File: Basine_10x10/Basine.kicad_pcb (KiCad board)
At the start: 2 copper layers, 100 x 100 mm, 98 parts, among them J1 2060-451/998-404, J10 2060-451/998-404, J11 2060-451/998-404, J12 2060-451/998-404, J13 2060-451/998-404, J14 2060-451/998-404, J15 2060-451/998-404, J16 2060-451/998-404, J2 2060-451/998-404, J3 2060-451/998-404, J4 2060-451/998-404, J5 2060-451/998-404, J6 2060-451/998-404, J7 2060-451/998-404, J8 2060-451/998-404, J9 2060-451/998-404, U1 SRV05-4, U17 TPS5430DDA, U4 SN65HVD230

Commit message: 10x10
tentative de fabrication
pénurie spring clamp à gérer
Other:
- board text added: "0V"
- board text added: "24V"
- board text added: "3V3"
- board text added: "5V"
- board text added: "CAN"
- board text added: "H"
- board text added: "L"

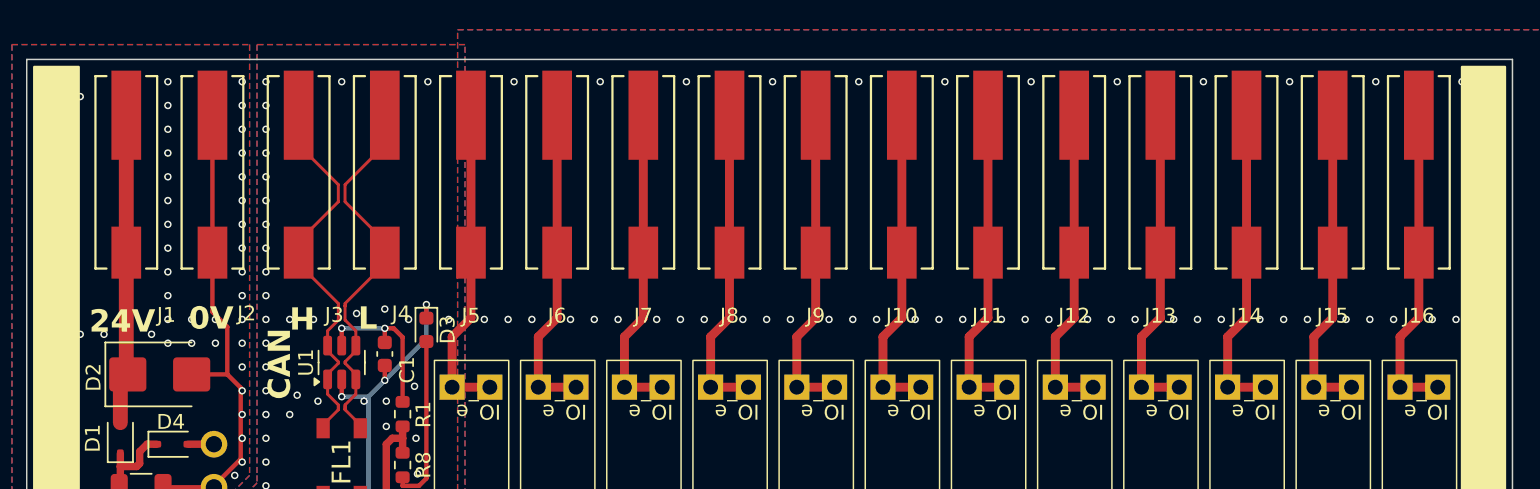
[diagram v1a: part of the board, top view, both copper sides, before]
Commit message: 10x10
chgt connecteur wago
fabrication
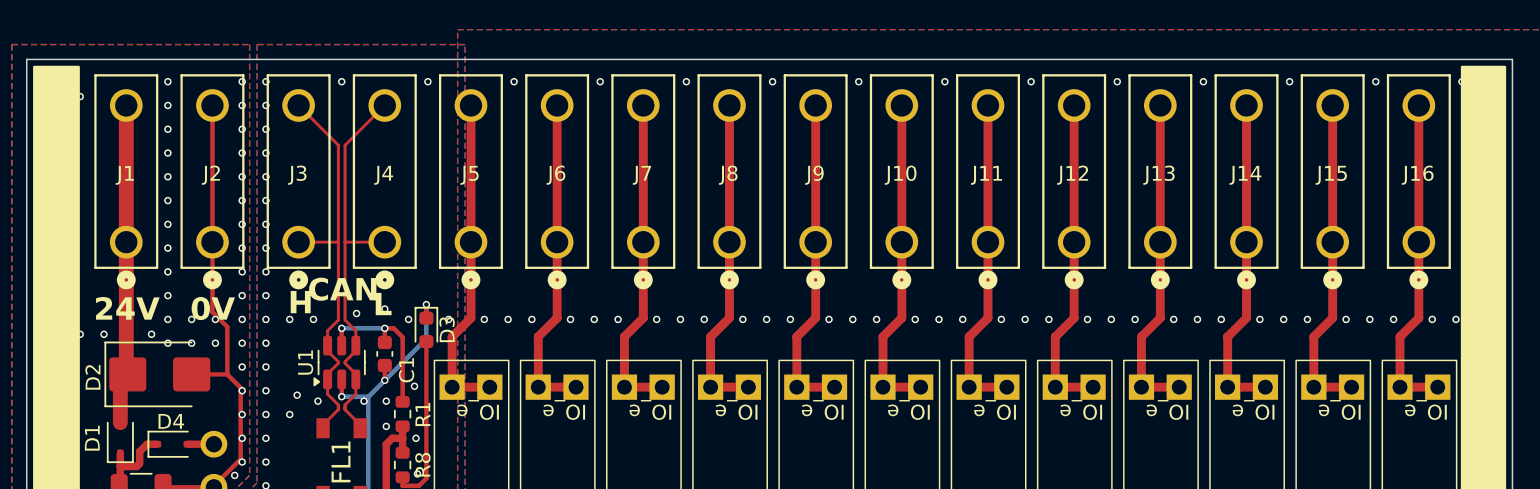
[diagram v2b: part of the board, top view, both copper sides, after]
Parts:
- J1, J10, J11, J12, J13, J14, J15, J16, J2, J3, J4, J5, J6, J7, J8, J9: footprint Chimere_comps:CONN_2060-451_998-404_WAGO -> Chimere_comps:CONN_2060-1451_998-404_WAGO
- moved J10 4.70 mm to (158.9, 112.3), turned to 0 degrees
- moved J5 4.70 mm to (129.9, 112.3), turned to 0 degrees
- moved J6 4.70 mm to (135.7, 112.3), turned to 0 degrees
- moved J7 4.70 mm to (141.5, 112.3), turned to 0 degrees
- moved J8 4.70 mm to (147.3, 112.3), turned to 0 degrees
- moved J9 4.70 mm to (153.1, 112.3), turned to 0 degrees
- moved J1 4.70 mm to (106.7, 112.3), turned to 0 degrees
- moved J11 4.70 mm to (164.7, 112.3), turned to 0 degrees
- moved J12 4.70 mm to (170.5, 112.3), turned to 0 degrees
- moved J13 4.70 mm to (176.3, 112.3), turned to 0 degrees
- moved J14 4.70 mm to (182.1, 112.3), turned to 0 degrees
- moved J15 4.70 mm to (187.9, 112.3), turned to 0 degrees
- moved J16 4.70 mm to (193.7, 112.3), turned to 0 degrees
- moved J2 4.70 mm to (112.5, 112.3), turned to 0 degrees
- moved J3 4.70 mm to (118.3, 112.3), turned to 0 degrees
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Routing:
- net CAN_N: track 26.3 -> 27.4 mm
- net CAN_P: track 26.3 -> 27.4 mm
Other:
- board text removed: "CAN_H"
- board text removed: "CAN_L"

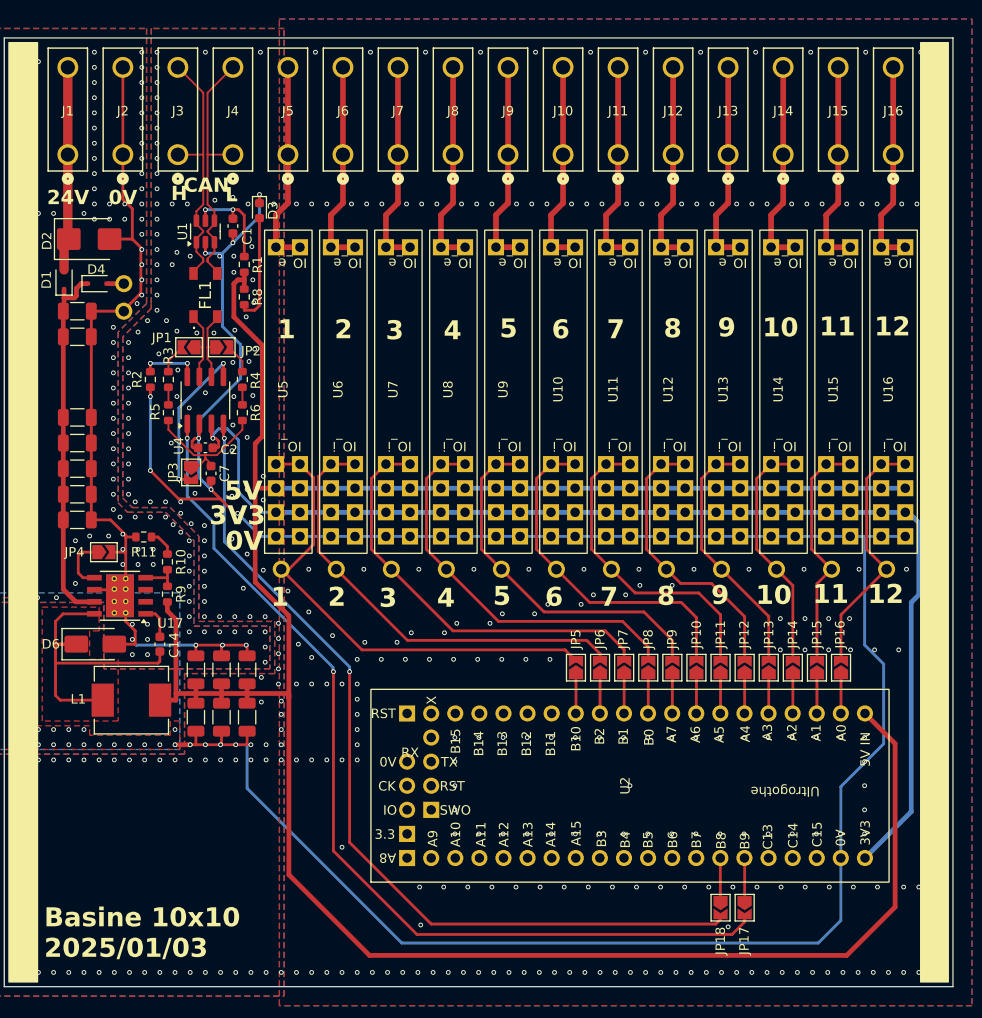
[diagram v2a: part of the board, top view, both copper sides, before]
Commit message: passage au pas de 2,54mm pour toutes les allumettes
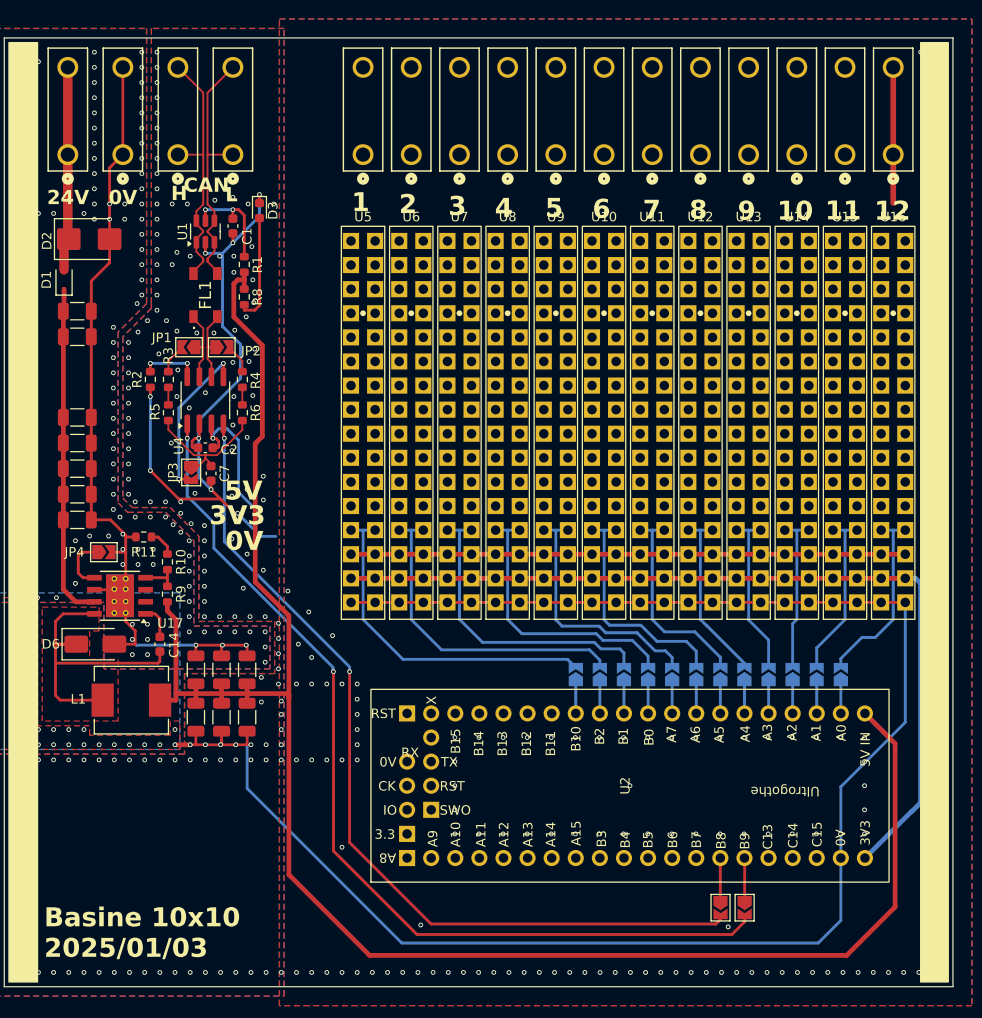
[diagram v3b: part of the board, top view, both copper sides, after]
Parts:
- removed D4: 1N5819WS, Diode_SMD:D_SOD-323
- removed TP1, TP10, TP11, TP12, TP13, TP14, TP2, TP3, TP4, TP5, TP6, TP7, TP8, TP9: TestPoint, Chimere_comps:Pastille
- JP10, JP11, JP12, JP13, JP14, JP15, JP16, JP5, JP6, JP7, JP8, JP9: moved to B.Cu
- moved U5 10.5 mm to (137.8, 144.3)
- moved U6 10.0 mm to (142.9, 144.3)
- moved U7 9.51 mm to (148.0, 144.3)
- moved U8 9.03 mm to (153.1, 144.3)
- moved U9 8.59 mm to (158.1, 144.3)
- moved U10 8.19 mm to (163.2, 144.3)
- moved J5 7.92 mm to (137.8, 112.3)
- moved U11 7.84 mm to (168.3, 144.3)
- moved U12 7.53 mm to (173.4, 144.3)
- moved U13 7.29 mm to (178.5, 144.3)
- moved J6 7.20 mm to (142.9, 112.3)
- moved U14 7.11 mm to (183.5, 144.3)
- moved U15 7.00 mm to (188.6, 144.3)
- moved U16 6.96 mm to (193.7, 144.3)
- moved J7 6.48 mm to (148.0, 112.3)
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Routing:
- net Net-(J7-Pin_1): track 21.4 -> 0.00 mm
- net Net-(J12-Pin_1): track 21.4 -> 0.00 mm
- net Net-(J8-Pin_1): track 21.4 -> 0.00 mm
- net Net-(J5-Pin_1): track 21.4 -> 0.00 mm
- net Net-(J15-Pin_1): track 21.4 -> 0.00 mm
- net Net-(J13-Pin_1): track 21.4 -> 0.00 mm
- net Net-(J10-Pin_1): track 21.4 -> 0.00 mm
- net Net-(J9-Pin_1): track 21.4 -> 0.00 mm
- net Net-(J6-Pin_1): track 21.4 -> 0.00 mm
- net Net-(J14-Pin_1): track 21.4 -> 0.00 mm
- net Net-(J11-Pin_1): track 21.4 -> 0.00 mm
- net 0V: track 356.8 -> 336.8 mm, vias 606 -> 490
- net 3V3: track 123.7 -> 107.6 mm
- net Net-(JP5-B): track 51.1 -> 36.5 mm
- net Net-(JP6-B): track 47.2 -> 34.4 mm
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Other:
- board text removed: "+"
- board text removed: "-"
- board text removed: "autre source"

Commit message: Basine 10x10 : enlever DCDC et CAN
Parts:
- removed C1, C2: 100nF 50V X7R, Capacitor_SMD:C_0603_1608Metric
- removed C10, C11, C15, C18, C19, C3, C4, C8, C9: 10uF 50V, Capacitor_SMD:C_1206_3216Metric
- removed C12, C13, C16, C17: 47uF 10V X5R, Capacitor_SMD:C_1206_3216Metric
- removed C14, C7: 10nF 50V X7R, Capacitor_SMD:C_0603_1608Metric
- removed D1: 1N5819WS, Diode_SMD:D_SOD-323
- removed D2: SMBJ30CA, Diode_SMD:D_SMB
- removed D3: LED, LED_SMD:LED_0603_1608Metric
- removed D6: SS54, Diode_SMD:D_SMA
- removed FL1: ~, Chimere_comps:ACT45B1012PTL003
- removed JP1, JP2, JP3, JP4: SolderJumper_2_Open, Jumper:SolderJumper-2_P1.3mm_Open_TrianglePad1.0x1.5mm
- removed L1: SMMS0650-680M, Inductor_SMD:L_Chilisin_BMRB00060650
- removed R1: 1k, Resistor_SMD:R_0603_1608Metric
- removed R10: 470, Resistor_SMD:R_0603_1608Metric
- removed R11: 2k7, Resistor_SMD:R_0603_1608Metric
- removed R2, R8, R9: 10k, Resistor_SMD:R_0603_1608Metric
- removed R3, R4: 33, Resistor_SMD:R_0603_1608Metric
- removed R5, R6: 27, Resistor_SMD:R_0603_1608Metric
- removed U1: SRV05-4, Package_TO_SOT_SMD:SOT-23-6
- removed U4: SN65HVD230, Package_SO:SOIC-8_3.9x4.9mm_P1.27mm
- added J17: 2060-451/998-404, Chimere_comps:CONN_2060-1451_998-404_WAGO, F.Cu at (188.1, 112.3)
- added J18: 2060-451/998-404, Chimere_comps:CONN_2060-1451_998-404_WAGO, F.Cu at (193.2, 112.3)
- added JP19: SolderJumper_2_Open, Jumper:SolderJumper-2_P1.3mm_Open_TrianglePad1.0x1.5mm, F.Cu at (44.2, 147.0)
- added JP20: SolderJumper_2_Open, Jumper:SolderJumper-2_P1.3mm_Open_TrianglePad1.0x1.5mm, F.Cu at (44.2, 150.5)
- added U18: ~, Chimere_mods:Allumette, F.Cu at (59.7, 135.9)
- added U19: ~, Chimere_mods:Allumette, F.Cu at (59.7, 142.1)
- added U20: ~, Chimere_mods:Allumette, F.Cu at (73.0, 85.5)
- JP10, JP11, JP12, JP13, JP14, JP15, JP16, JP5, JP6, JP7, JP8, JP9: moved to F.Cu
- U17: value TPS5430DDA -> ~; footprint Package_SO:TI_SO-PowerPAD-8_ThermalVias -> Chimere_mods:Allumette
- moved JP17 146.2 mm to (66.2, 97.4), turned to 0 degrees
- moved JP16 142.2 mm to (66.2, 93.9), turned to 0 degrees
- moved JP18 142.0 mm to (66.2, 101.0), turned to 0 degrees
- moved JP15 142.0 mm to (66.2, 90.3), turned to 0 degrees
- moved JP14 136.4 mm to (61.9, 104.5), turned to 0 degrees
- moved JP13 135.9 mm to (61.9, 101.0), turned to 0 degrees
- moved JP12 135.4 mm to (61.9, 97.4), turned to 0 degrees
- moved JP11 135.1 mm to (61.9, 93.9), turned to 0 degrees
- moved JP10 135.0 mm to (61.9, 90.3), turned to 0 degrees
- moved JP9 129.0 mm to (57.5, 104.5), turned to 0 degrees
- moved JP8 128.6 mm to (57.5, 101.0), turned to 0 degrees
- moved JP7 128.3 mm to (57.5, 97.4), turned to 0 degrees
- moved JP5 128.2 mm to (57.5, 90.3), turned to 0 degrees
- moved JP6 128.2 mm to (57.5, 93.9), turned to 0 degrees
- moved U17 88.6 mm to (73.0, 79.3), turned to 0 degrees
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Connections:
- J3 pad 1: CAN_P -> Net-(J3-Pin_1)
- J4 pad 1: CAN_N -> Net-(J4-Pin_1)
- JP17 pad 1: Net-(JP17-A) -> unconnected-(JP17-A-Pad1)
- JP17 pad 2: CAN_TX -> Net-(JP17-B)
- JP18 pad 1: Net-(JP18-A) -> unconnected-(JP18-A-Pad1)
- JP18 pad 2: CAN_RX -> Net-(JP18-B)
- U17 pad 1: Net-(U17-BOOT) -> 0V
- U17 pad 2: unconnected-(U17-NC-Pad2) -> 3V3
- U17 pad 3: unconnected-(U17-NC-Pad3) -> 5V
- U17 pad 4: /s_ALIM_5V/Vsense -> Net-(JP17-B)
- U17 pad 5: /s_ALIM_5V/EN_i -> Net-(J17-Pin_1)
- U17 pad 6: 0V -> (no net)
- U17 pad 7: /s_ALIM_5V/Vs_f -> (no net)
- U17 pad 8: /s_ALIM_5V/ph -> (no net)
- U17 pad 9: 0V -> (no net)
- U2 pad 14: Net-(JP18-A) -> CAN_RX
- U2 pad 15: Net-(JP17-A) -> CAN_TX
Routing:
- net 0V: track 336.8 -> 58.4 mm, vias 490 -> 181
- net 5V: track 248.9 -> 58.4 mm
- net CAN_TX: track 99.7 -> 0.00 mm, vias 2 -> 0
- net CAN_RX: track 93.0 -> 0.00 mm, vias 2 -> 0
- net 3V3: track 107.6 -> 58.4 mm, vias 1 -> 0
- net /s_ALIM_5V/Vs_f: track 35.0 -> 0.00 mm
- net /s_ALIM_5V/ph: track 34.7 -> 0.00 mm
- net CAN_N: track 27.4 -> 0.00 mm
- net CAN_P: track 27.4 -> 0.00 mm
- net Net-(JP5-B): track 36.5 -> 12.0 mm
- net Net-(JP6-B): track 34.4 -> 12.0 mm
- net 24V: track 20.9 -> 0.00 mm
- net Net-(JP7-B): track 32.3 -> 12.0 mm
- net Net-(JP8-B): track 29.6 -> 12.0 mm
- net /s_CAN/Vref_can: track 16.8 -> 0.00 mm, vias 2 -> 0
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- removed copper zone on F.Cu, net /s_ALIM_5V/ph
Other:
- board text added: "VIN"
- board text removed: "24V"
- board text removed: "CAN"
- board text removed: "H"
- board text removed: "L"

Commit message: Basine_10x10 : placement et routage
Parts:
- removed JP19, JP20: SolderJumper_2_Open, Jumper:SolderJumper-2_P1.3mm_Open_TrianglePad1.0x1.5mm
- removed U20: ~, Chimere_mods:Allumette
- added JP1: SolderJumper_2_Open, Jumper:SolderJumper-2_P1.3mm_Open_TrianglePad1.0x1.5mm, B.Cu at (106.8, 169.3)
- added JP2: SolderJumper_2_Open, Jumper:SolderJumper-2_P1.3mm_Open_TrianglePad1.0x1.5mm, B.Cu at (111.9, 169.3)
- added JP3: SolderJumper_2_Open, Jumper:SolderJumper-2_P1.3mm_Open_TrianglePad1.0x1.5mm, B.Cu at (117.0, 169.3)
- added JP4: SolderJumper_2_Open, Jumper:SolderJumper-2_P1.3mm_Open_TrianglePad1.0x1.5mm, B.Cu at (122.1, 169.3)
- added U1: ~, Chimere_mods:Allumette, F.Cu at (106.8, 142.3)
- added U3: ~, Chimere_mods:Allumette, F.Cu at (117.0, 142.3)
- added U4: ~, Chimere_mods:Allumette, F.Cu at (122.1, 142.3)
- JP10, JP11, JP12, JP13, JP14, JP15, JP16, JP17, JP18, JP5, JP6, JP7, JP8, JP9: moved to B.Cu
- U19: footprint Chimere_mods:Allumette -> Chimere_mods:Ultrogothe
- U2: footprint Chimere_mods:Ultrogothe -> Chimere_mods:Allumette
- moved JP18 144.2 mm to (193.2, 169.3), turned to 90 degrees
- moved JP17 141.5 mm to (188.1, 169.3), turned to 90 degrees
- moved JP16 139.0 mm to (183.0, 169.3), turned to 90 degrees
- moved JP15 136.8 mm to (177.9, 169.3), turned to 90 degrees
- moved U18 133.6 mm to (193.2, 142.3)
- moved U17 131.2 mm to (188.1, 142.3)
- moved JP14 128.5 mm to (172.8, 169.3), turned to 90 degrees
- moved JP13 126.0 mm to (167.8, 169.3), turned to 90 degrees
- moved JP12 123.8 mm to (162.7, 169.3), turned to 90 degrees
- moved JP11 121.9 mm to (157.6, 169.3), turned to 90 degrees
- moved JP10 120.2 mm to (152.5, 169.3), turned to 90 degrees
- moved JP9 110.8 mm to (147.5, 169.3), turned to 90 degrees
- moved JP8 108.9 mm to (142.4, 169.3), turned to 90 degrees
- moved JP7 107.3 mm to (137.3, 169.3), turned to 90 degrees
- moved JP6 106.1 mm to (132.2, 169.3), turned to 90 degrees
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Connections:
- J1 pad 1: 24V -> VIN
- JP10 pad 1: A6 -> B1
- JP11 pad 1: A5 -> A7
- JP12 pad 1: A4 -> A6
- JP13 pad 1: A3 -> A5
- JP14 pad 1: A2 -> A4
- JP15 pad 1: A1 -> A3
- JP16 pad 1: A0 -> A2
- JP17 pad 1: unconnected-(JP17-A-Pad1) -> A1
- JP18 pad 1: unconnected-(JP18-A-Pad1) -> A0
- JP5 pad 1: B10 -> B13
- JP6 pad 1: B2 -> B12
- JP7 pad 1: B1 -> B11
- JP8 pad 1: B0 -> B10
- JP9 pad 1: A7 -> B2
- U10 pad 5: Net-(J10-Pin_1) -> (no net)
- U11 pad 5: Net-(J11-Pin_1) -> (no net)
- U12 pad 5: Net-(J12-Pin_1) -> (no net)
- U13 pad 5: Net-(J13-Pin_1) -> (no net)
- U14 pad 5: Net-(J14-Pin_1) -> (no net)
- U15 pad 5: Net-(J15-Pin_1) -> (no net)
- U16 pad 5: Net-(J16-Pin_1) -> (no net)
- U17 pad 5: Net-(J17-Pin_1) -> (no net)
- U18 pad 4: Net-(JP19-B) -> Net-(JP18-B)
- U18 pad 5: Net-(J4-Pin_1) -> (no net)
- U19 pad 1: 0V -> unconnected-(U19-A8-Pad1)
- U19 pad 10: (no net) -> unconnected-(U19-B4-Pad10)
- U19 pad 11: (no net) -> unconnected-(U19-B5-Pad11)
- U19 pad 12: (no net) -> unconnected-(U19-B6-Pad12)
- U19 pad 13: (no net) -> unconnected-(U19-B7-Pad13)
- U19 pad 14: (no net) -> CAN_RX
- U19 pad 15: (no net) -> CAN_TX
- U19 pad 16: (no net) -> unconnected-(U19-C13-Pad16)
- U19 pad 2: 3V3 -> unconnected-(U19-A9-Pad2)
- U19 pad 3: 5V -> unconnected-(U19-A10-Pad3)
- U19 pad 4: Net-(JP20-B) -> unconnected-(U19-A11-Pad4)
- U19 pad 5: Net-(J3-Pin_1) -> unconnected-(U19-A12-Pad5)
- U19 pad 6: (no net) -> unconnected-(U19-A13-Pad6)
- U19 pad 7: (no net) -> unconnected-(U19-A14-Pad7)
- U19 pad 8: (no net) -> unconnected-(U19-A15-Pad8)
- U19 pad 9: (no net) -> unconnected-(U19-B3-Pad9)
- U2 pad 1: unconnected-(U2-A8-Pad1) -> 0V
- U2 pad 10: unconnected-(U2-B4-Pad10) -> (no net)
- U2 pad 11: unconnected-(U2-B5-Pad11) -> (no net)
- U2 pad 12: unconnected-(U2-B6-Pad12) -> (no net)
- U2 pad 13: unconnected-(U2-B7-Pad13) -> (no net)
- U2 pad 14: CAN_RX -> (no net)
- U2 pad 15: CAN_TX -> (no net)
- U2 pad 16: unconnected-(U2-C13-Pad16) -> (no net)
- U2 pad 17: unconnected-(U2-C14-Pad17) -> (no net)
- U2 pad 2: unconnected-(U2-A9-Pad2) -> 3V3
- U2 pad 20: 3V3 -> VIN
- U2 pad 3: unconnected-(U2-A10-Pad3) -> 5V
- U2 pad 4: unconnected-(U2-A11-Pad4) -> Net-(JP2-B)
- U2 pad 5: unconnected-(U2-A12-Pad5) -> (no net)
- U2 pad 6: unconnected-(U2-A13-Pad6) -> (no net)
- U2 pad 7: unconnected-(U2-A14-Pad7) -> (no net)
- U2 pad 8: unconnected-(U2-A15-Pad8) -> (no net)
- U2 pad 9: unconnected-(U2-B3-Pad9) -> (no net)
- U5 pad 5: Net-(J5-Pin_1) -> (no net)
- U6 pad 5: Net-(J6-Pin_1) -> (no net)
- U7 pad 5: Net-(J7-Pin_1) -> (no net)
- U8 pad 5: Net-(J8-Pin_1) -> (no net)
- U9 pad 5: Net-(J9-Pin_1) -> (no net)
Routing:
- net 0V: track 58.4 -> 489.5 mm, vias 181 -> 184
- net VIN: track 0.00 -> 106.5 mm
- net CAN_RX: track 0.00 -> 68.9 mm, vias 0 -> 1
- net 3V3: track 58.4 -> 126.2 mm
- net CAN_TX: track 0.00 -> 66.7 mm, vias 0 -> 2
- net 5V: track 58.4 -> 120.8 mm
- net B15: track 0.00 -> 30.9 mm
- net B14: track 0.00 -> 28.3 mm
- net Net-(J3-Pin_1): track 0.00 -> 22.7 mm
- net Net-(J6-Pin_1): track 0.00 -> 22.6 mm
- net Net-(J15-Pin_1): track 0.00 -> 22.6 mm
- net Net-(J13-Pin_1): track 0.00 -> 22.6 mm
- net Net-(J9-Pin_1): track 0.00 -> 22.6 mm
- net Net-(J8-Pin_1): track 0.00 -> 22.6 mm
- net Net-(J7-Pin_1): track 0.00 -> 22.6 mm
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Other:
- board text added: "13"
- board text added: "14"
- board text added: "15"
- board text added: "16"
- board text added: "Basine 10x10 2025/05/01"
- board text added: "EXT"
- board text added: "INT"
- board text removed: "Basine 10x10 2025/01/03"
